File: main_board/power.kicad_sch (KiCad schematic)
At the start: 30 parts, among them J10 B5B-XH, J11 B5B-XH, J12 B3B-XH, J13 B5B-XH, J8 Conn_01x02, J9 Conn_01x02, Q10 DTC114E, Q9 DTC114E, U12 OKL-T/6-W12N-C, U13 XC6221B332MR, U14 FT232RL, U15 SL2.1A, Y1 12MHz

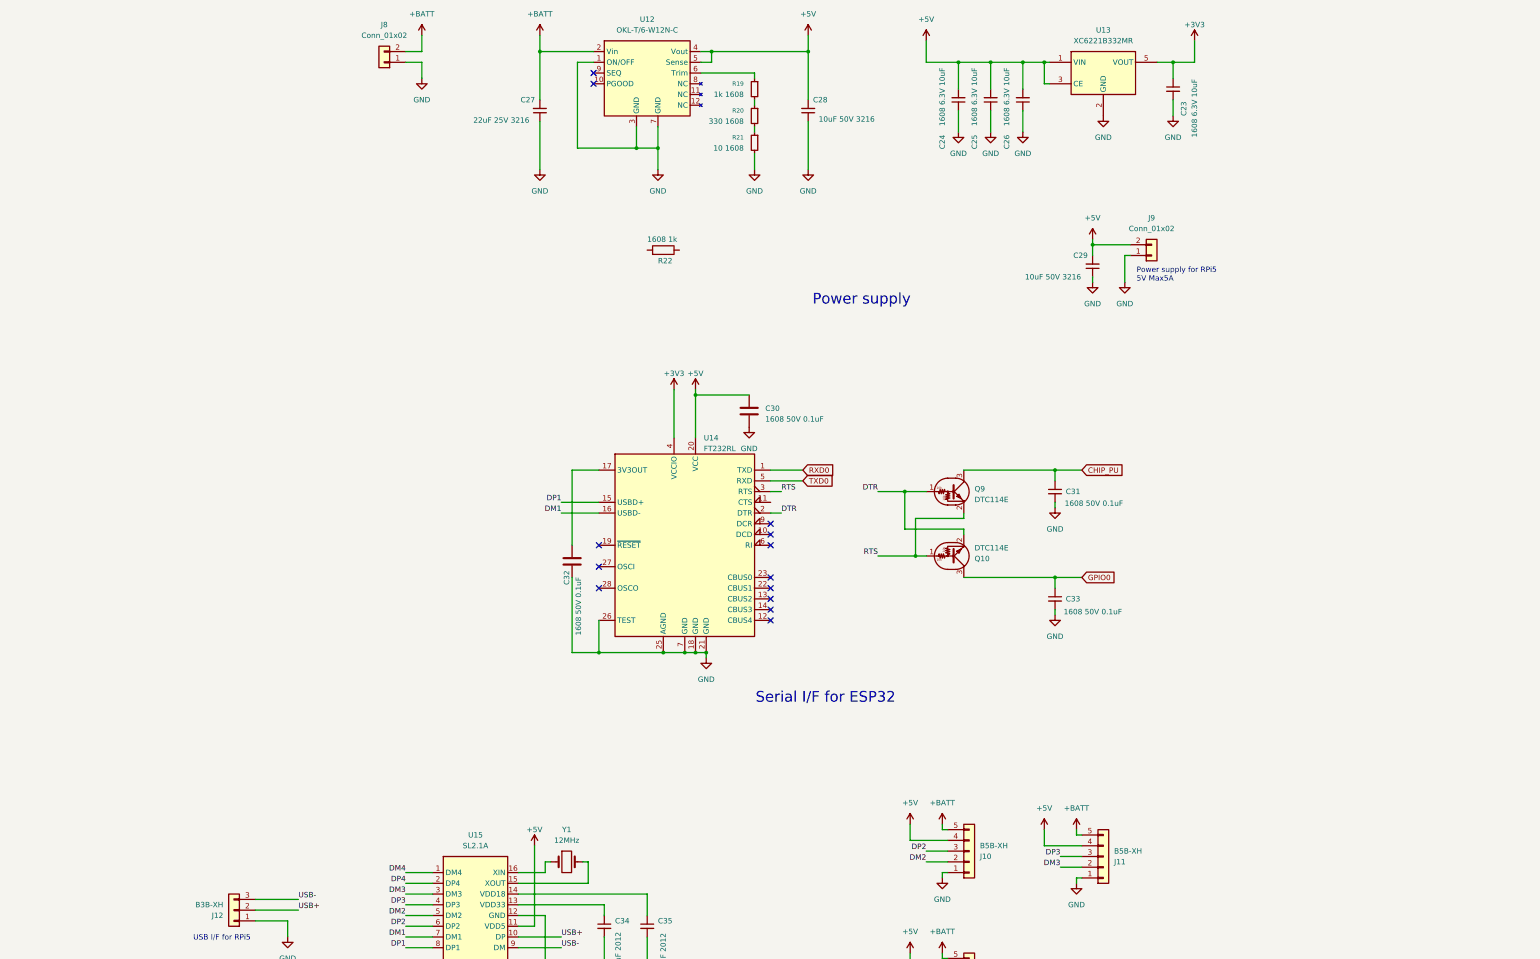
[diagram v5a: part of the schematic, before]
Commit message: 充電回路追加
Signed-off-by: Kazuki Iida <elkel53930@gmail.com>
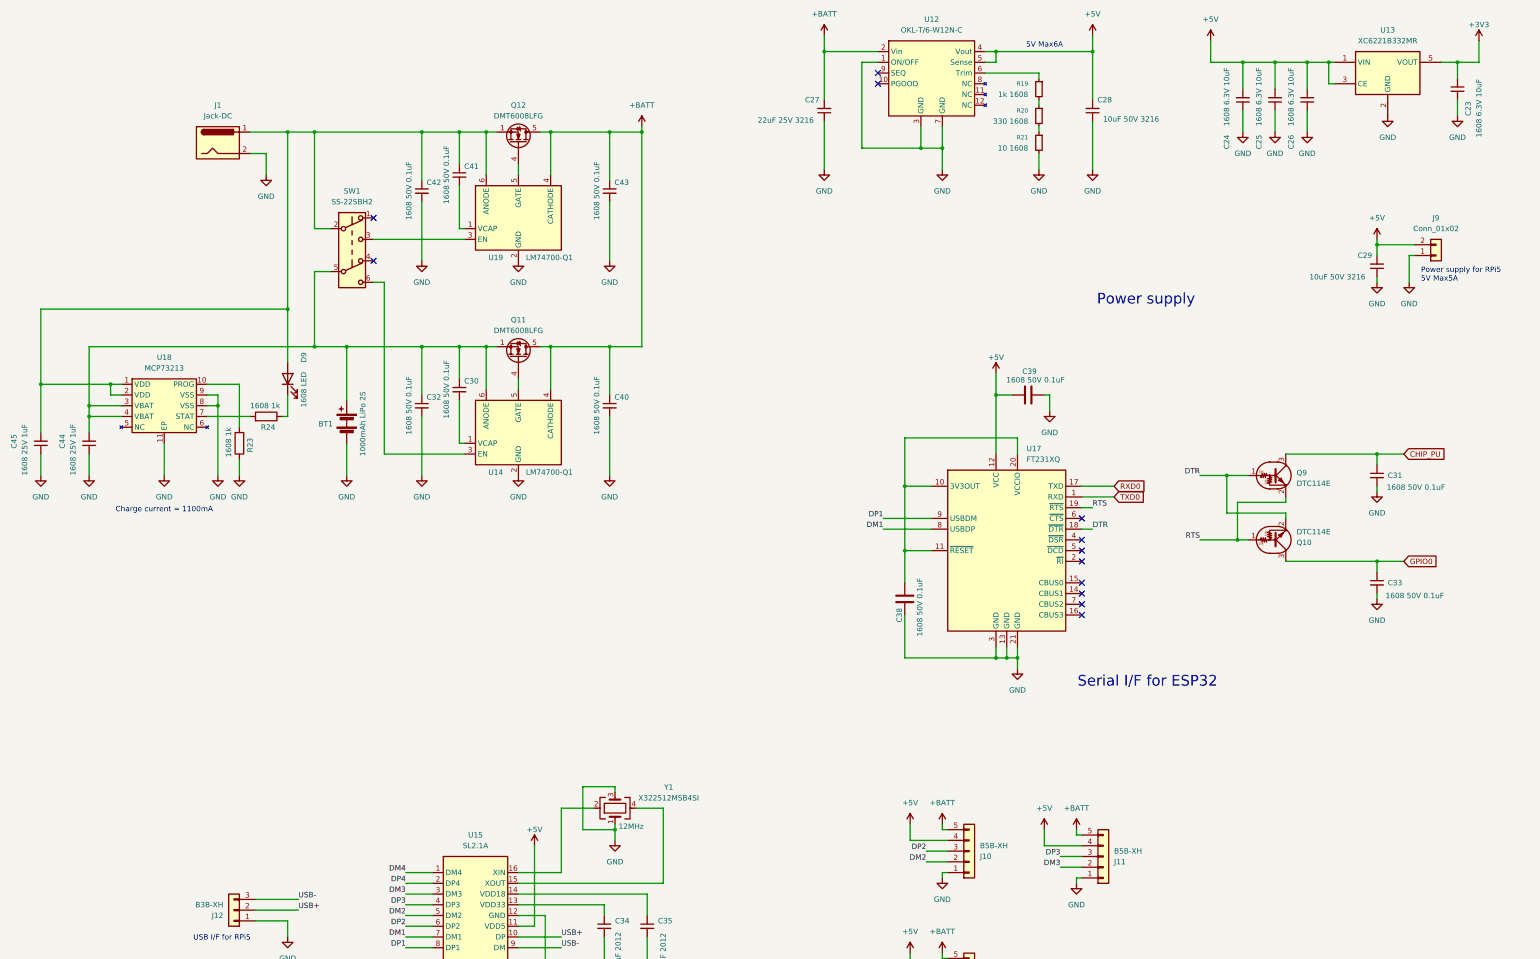
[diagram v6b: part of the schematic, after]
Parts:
- removed C30, C32: 1608 50V 0.1uF, Capacitor_SMD:C_0603_1608Metric, symbol Device:C
- removed J8: Conn_01x02, Library:PowerCable, symbol Connector_Generic:Conn_01x02
- removed R22: 1608 1k, Resistor_SMD:R_0603_1608Metric, symbol Device:R
- removed U14: FT232RL, Package_SO:SSOP-28_5.3x10.2mm_P0.65mm, symbol Interface_USB:FT232RL
- removed Y1: 12MHz, Crystal:Crystal_HC49-4H_Vertical, symbol Device:Crystal
- added BT1: 1000mAh LiPo 2S, symbol Device:Battery
- added C30, C32, C40, C41, C42, C43: 1608 50V 0.1uF, Capacitor_SMD:C_0603_1608Metric, symbol Device:C_Small
- added C38, C39: 1608 50V 0.1uF, Capacitor_SMD:C_0603_1608Metric, symbol Device:C
- added C44, C45: 1608 25V 1uF, Capacitor_SMD:C_0603_1608Metric, symbol Device:C_Small
- added D9: 1608 LED, LED_SMD:LED_0603_1608Metric, symbol Device:LED
- added J1: Jack-DC, symbol Connector:Jack-DC
- added Q11, Q12: DMT6008LFG, Package_SON:Diodes_PowerDI3333-8, symbol Transistor_FET:DMT6008LFG
- added R23, R24: 1608 1k, Resistor_SMD:R_0603_1608Metric, symbol Device:R
- added SW1: SS-22SBH2, symbol Switch:SW_Push_DPDT
- added U14, U19: LM74700-Q1, Package_TO_SOT_SMD:SOT-23-6, symbol Power_Management:LM74700
- added U17: FT231XQ, Package_DFN_QFN:QFN-20-1EP_4x4mm_P0.5mm_EP2.5x2.5mm, symbol Interface_USB:FT231XQ
- added U18: MCP73213, Package_DFN_QFN:DFN-10-1EP_3x3mm_P0.5mm_EP1.58x2.35mm, symbol micromouse-twilight:MCP73213
- added Y1: X322512MSB4SI, Crystal:Crystal_SMD_3225-4Pin_3.2x2.5mm, symbol Device:Crystal_GND24
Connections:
- net +5V: now also C39.1, U17.12 (VCC)
- net +BATT: now also C40.1, C43.1, Q11.5 (D), Q12.5 (D), U14.4 (CATHODE), U19.4 (CATHODE)
- net DM1: now also U17.8 (USBDP)
- net DP1: now also U17.9 (USBDM)
- net DTR: now also U17.18 (~{DTR})
- net GND: now also BT1.2 (-), C32.2, C38.2, C39.2, C40.2, C42.2, C43.2, C44.1, C45.1, J1.2, R23.1, U14.2 (GND), U17.13 (GND), U17.21 (GND), U17.3 (GND), U18.11 (EP), U18.8 (VSS), U18.9 (VSS), U19.2 (GND), Y1.1, Y1.3
- net RTS: now also U17.19 (~{RTS})
- net RXD0: now also U17.17 (TXD)
- net TXD0: now also U17.1 (RXD)
- net at U15.16 (XIN): now also Y1.2
- net at U15.15 (XOUT): now also Y1.4
- new net: BT1.1 (+), C30.1, C32.1, C44.2, Q11.1 (S), Q11.2 (S), Q11.3 (S), SW1.5 (B), U14.6 (ANODE), U18.3 (VBAT), U18.4 (VBAT)
- new net: C41.1, C42.1, C45.2, D9.2 (A), J1.1, Q12.1 (S), Q12.2 (S), Q12.3 (S), SW1.2 (B), U18.1 (VDD), U18.2 (VDD), U19.6 (ANODE)
- new net: Q11.4 (G), U14.5 (GATE)
- new net: C41.2, U19.1 (VCAP)
- new net: C38.1, U17.10 (3V3OUT), U17.11 (~{RESET}), U17.20 (VCCIO)
- new net: SW1.3 (C), U19.3 (EN)
- new net: Q12.4 (G), U19.5 (GATE)
- new net: D9.1 (K), R24.1
- new net: R23.2, U18.10 (PROG)
- new net: R24.2, U18.7 (STAT)
- new net: SW1.6 (C), U14.3 (EN)
- new net: C30.2, U14.1 (VCAP)
- no-connect marks 13 -> 12
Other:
- note added: "5V Max6A"
- note added: "Charge current = 1100mA"
- moved on the sheet: C23, C24, C25, C26, C27, C28, C29, C31, C33, J9, Q10, Q9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

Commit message: 部品名追加
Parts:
- removed C38, C39: 1608 50V 0.1uF, Capacitor_SMD:C_0603_1608Metric, symbol Device:C
- removed C44, C45: 1608 25V 1uF, Capacitor_SMD:C_0603_1608Metric, symbol Device:C_Small
- removed D9: 1608 LED, LED_SMD:LED_0603_1608Metric, symbol Device:LED
- removed J1: Jack-DC, symbol Connector:Jack-DC
- removed J10, J11, J13: B5B-XH, Connector_JST:JST_XH_B5B-XH-A_1x05_P2.50mm_Vertical, symbol Connector_Generic:Conn_01x05
- removed J12: B3B-XH, Connector_JST:JST_XH_B3B-XH-A_1x03_P2.50mm_Vertical, symbol Connector_Generic:Conn_01x03
- removed R19: 1k 1608, Resistor_SMD:R_0603_1608Metric, symbol Device:R_Small
- removed R20: 330 1608, Resistor_SMD:R_0603_1608Metric, symbol Device:R_Small
- removed R21: 10 1608, Resistor_SMD:R_0603_1608Metric, symbol Device:R_Small
- removed R23, R24: 1608 1k, Resistor_SMD:R_0603_1608Metric, symbol Device:R
- added C36, C37: CL10A105KB8NNNC, Capacitor_SMD:C_0603_1608Metric, symbol Device:C_Small
- added C38, C39: CC0603KRX7R9BB104, Capacitor_SMD:C_0603_1608Metric, symbol Device:C_Small
- added D8: KT-0603R, LED_SMD:LED_0603_1608Metric, symbol Device:LED
- added D9: 1N5819WS, Diode_SMD:D_SOD-323, symbol Device:D_Schottky
- added J1: MJ-179PH, Library:PJ-002A, symbol Connector:Barrel_Jack_Switch
- added J10, J11, J2_, J8: B4B-ZR(LF)(SN), Connector_JST:JST_ZH_B4B-ZR_1x04_P1.50mm_Vertical, symbol Connector_Generic:Conn_01x04
- added J14, J15, J16: B2B-XH-A(LF)(SN), Connector_PinHeader_2.54mm:PinHeader_1x02_P2.54mm_Vertical, symbol Connector_Generic:Conn_01x02
- added R19, R22, R6: 0603WAF1001T5E, Resistor_SMD:R_0603_1608Metric, symbol Device:R
- added R20: 0603WAF3300T5E, Resistor_SMD:R_0603_1608Metric, symbol Device:R
- added R21: 0603WAF100JT5E, Resistor_SMD:R_0603_1608Metric, symbol Device:R
- C23, C24, C25, C26: value 1608 6.3V 10uF -> CL10A106KP8NNNC
- C27: value 22uF 25V 3216 -> CL21A106KAYNNNE; footprint Capacitor_SMD:C_1206_3216Metric -> Capacitor_SMD:C_0805_2012Metric
- C28, C29: value 10uF 50V 3216 -> CL21A106KAYNNNE; footprint Capacitor_SMD:C_1206_3216Metric -> Capacitor_SMD:C_0805_2012Metric
- C30, C31, C32, C33, C40, C41, C42, C43: value 1608 50V 0.1uF -> CC0603KRX7R9BB104
- C34, C35: value 10uF 2012 -> CL21A106KAYNNNE
- SW1: footprint (none) -> Library:SS-22SBH2
- U14, U19: value LM74700-Q1 -> LM74700QDBVRQ1
- U17: value FT231XQ -> FT231XQ-R
- U18: value MCP73213 -> MCP73213T-A6SI/MF
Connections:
- net +3V3: now also C23.2; no longer C23.1
- net +5V: now also C28.1, C29.1, C39.2, D9.2 (A), J10.1 (Pin_1), J11.1 (Pin_1), J2_.1 (Pin_1), J8.1 (Pin_1); no longer C28.2, C29.2
- net +BATT: now also C40.2, C43.2, D9.1 (K), J14.2 (Pin_2), J15.2 (Pin_2), J16.2 (Pin_2); no longer C40.1, C43.1
- net CHIP_PU: now also C31.2; no longer C31.1
- net DM2: now also J10.3 (Pin_3)
- net DM3: now also J11.3 (Pin_3)
- net DM4: now also J2_.3 (Pin_3)
- net DP2: now also J10.2 (Pin_2)
- net DP3: now also J11.2 (Pin_2)
- net DP4: now also J2_.2 (Pin_2)
- net GND: now also C23.1, C28.2, C29.2, C31.1, C33.1, C40.1, C41.1, C42.1, C43.1, C36.1, C37.1, C38.1, C39.1, J1.2, J1.3, J10.4 (Pin_4), J11.4 (Pin_4), J14.1 (Pin_1), J15.1 (Pin_1), J16.1 (Pin_1), J2_.4 (Pin_4), J8.4 (Pin_4), R19.2, R21.2; no longer C23.2, C28.1, C29.1, C31.2, C32.2, C33.2, C40.2, C42.2, C43.2
- net GPIO0: now also C33.2; no longer C33.1
- net USB+: now also J8.2 (Pin_2)
- net USB-: now also J8.3 (Pin_3)
- net at BT1.1 (+), Q11.1 (S), Q11.2 (S)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: now also C32.2, C42.2, C36.2; no longer C30.1, C32.1
- net at Q12.1 (S), Q12.2 (S), Q12.3 (S)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: now also C30.2, C41.2, C37.2, D8.2 (A), J1.1; no longer C41.1, C42.1
- net at U19.1 (VCAP): now also C30.1; no longer C41.2
- net at U17.10 (3V3OUT), U17.11 (~{RESET}), U17.20 (VCCIO): now also C38.2
- net at U18.10 (PROG): now also R19.1
- net at U18.7 (STAT): now also R22.1
- net at U14.1 (VCAP): now also C32.1; no longer C30.2
- net at U12.6 (Trim): now also R6.1
- new net: D8.1 (K), R22.2
- new net: R20.1, R6.2
- new net: R20.2, R21.1
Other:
- note added: "Power management"
- moved on the sheet: BT1, C34, J9, Q10, Q11, Q12, Q9, SW1, U13, U14, U15, U17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

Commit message: アートワーク開始
Signed-off-by: Kazuki Iida <elkel53930@gmail.com>
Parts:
- removed C34, C35: CL21A106KAYNNNE, Capacitor_SMD:C_0805_2012Metric, symbol Device:C_Small
- removed J10, J11, J2_: B4B-ZR(LF)(SN), Connector_JST:JST_ZH_B4B-ZR_1x04_P1.50mm_Vertical, symbol Connector_Generic:Conn_01x04
- removed U15: SL2.1A, Package_SO:SOP-16_3.9x9.9mm_P1.27mm, symbol Arduino_Motor_Driver:SL2.1A
- removed Y1: X322512MSB4SI, Crystal:Crystal_SMD_3225-4Pin_3.2x2.5mm, symbol Device:Crystal_GND24
- BT1: footprint (none) -> Library:Battery_Connector
- renumbered C41 to C23, C30 to C24, C43 to C25, C27 to C26, C29 to C27, C26 to C28, C25 to C29, C24 to C30, C23 to C31, C28 to C32, C42 to C33, C32 to C34, C40 to C35, C37 to C36, C36 to C37, C39 to C38, C31 to C39, C33 to C40, C38 to C41, D9 to D4, D8 to D5, J9 to J10, J14 to J11, J15 to J12, J16 to J13, J8 to J16, J1 to J9, Q12 to Q5, Q11 to Q6, Q9 to Q7, Q10 to Q8, R6 to R18, R20 to R19, R21 to R20, R22 to R21, R19 to R22, U19 to U14, U18 to U15, U14 to U16
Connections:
- net DM1 is gone; now on net USB+: U17.8 (USBDP)
- net DP1 is gone; now on net USB-: U17.9 (USBDM)
- net +5V: now also J10.1 (Pin_1); no longer J10.2 (Pin_2)
- net +BATT: now also J11.1 (Pin_1), J12.1 (Pin_1), J13.1 (Pin_1); no longer J11.2 (Pin_2), J12.2 (Pin_2), J13.2 (Pin_2)
- net GND: now also J10.2 (Pin_2), J11.2 (Pin_2), J12.2 (Pin_2), J13.2 (Pin_2); no longer J10.1 (Pin_1), J11.1 (Pin_1), J12.1 (Pin_1), J13.1 (Pin_1)
- net USB+: now also J16.3 (Pin_3); no longer J16.2 (Pin_2)
- net USB-: now also J16.2 (Pin_2); no longer J16.3 (Pin_3)
- net at U14.3 (EN): now also SW1.6 (C); no longer SW1.3 (C)
- net EXT_PWR: now reaches C23.2, C24.2, C36.2, D5.2 (A), J9.1, Q5.1 (S), Q5.2 (S), Q5.3 (S), SW1.2 (B), U14.6 (ANODE), U15.1 (VDD), U15.2 (VDD)
- net at U16.3 (EN): now also SW1.3 (C); no longer SW1.6 (C)
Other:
- note added: "USB-Serial I/F"
- note removed: "External I/F"
- note removed: "Serial I/F for ESP32"
- note removed: "USB Hub"
- moved on the sheet: BT1, C23, C24, C25, C26, C27, C28, C29, C30, C31, C32, C33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
